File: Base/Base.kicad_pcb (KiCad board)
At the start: 2 copper layers, 72.4 x 72.4 mm, 20 parts, among them J1 USB_C_Receptacle_USB2.0_16P, J2 JST_battery, J3 JST_header, J4 JST_speaker, J5 JST_debug, J6 JST_debug, SW1 SW_power, U1 MCP73831-2-OT, U2 MAX98357A

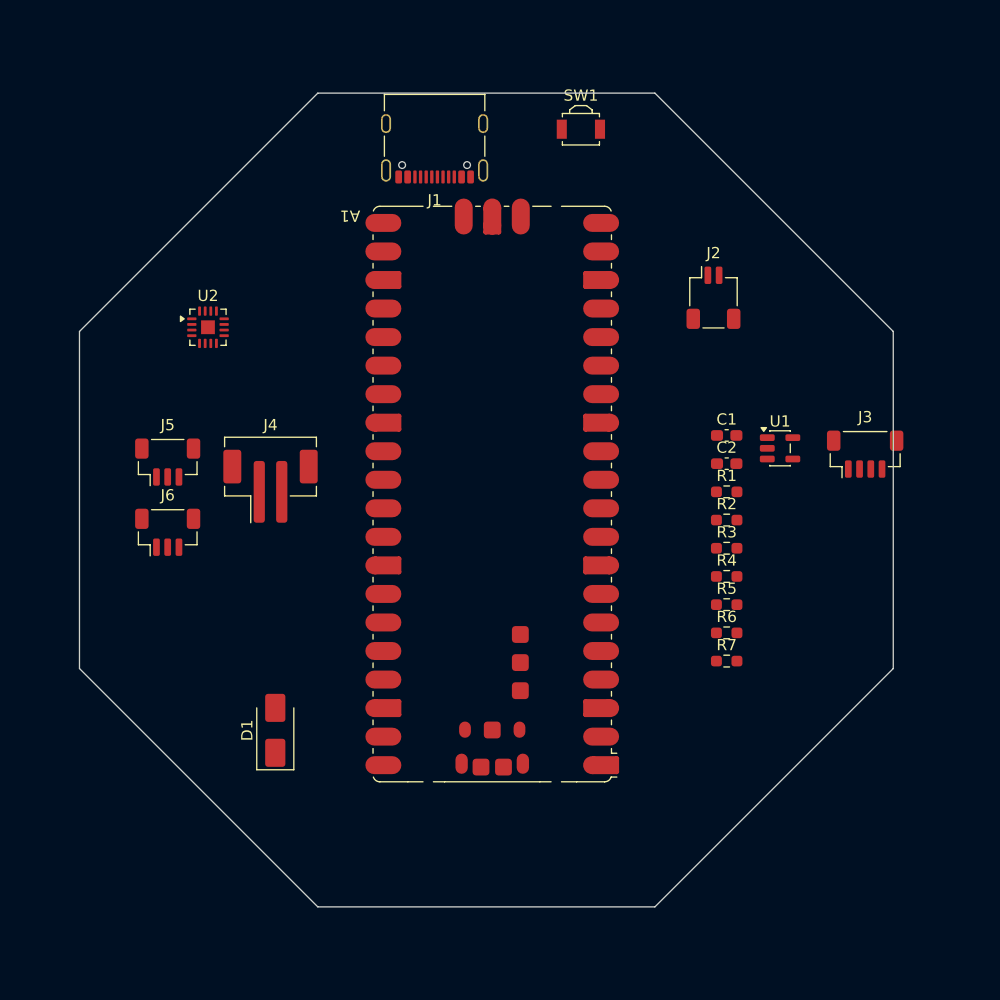
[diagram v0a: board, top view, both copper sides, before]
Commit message: Add LED files, finish base and LED schematics
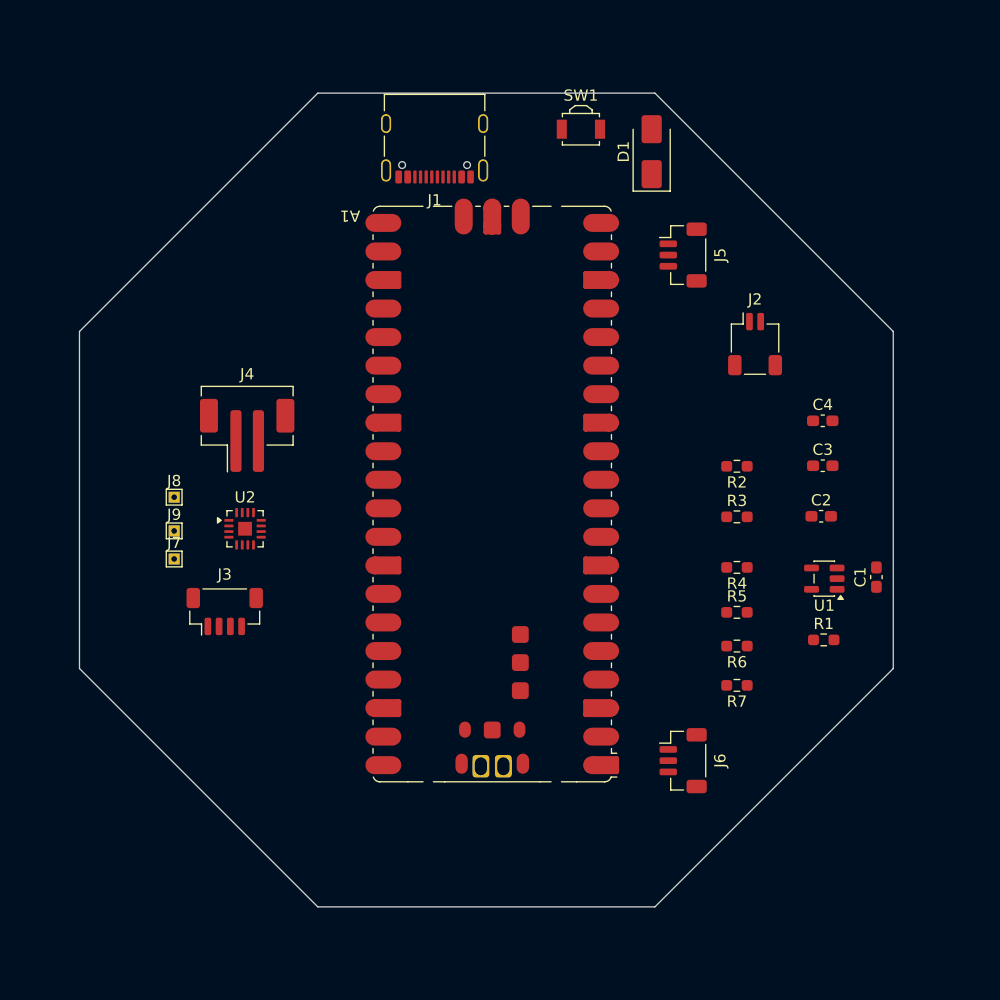
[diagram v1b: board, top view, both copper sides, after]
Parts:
- added C3: 4.7uF, Capacitor_SMD:C_0603_1608Metric_Pad1.08x0.95mm_HandSolder, F.Cu at (186.2, 99.5)
- added C4: 4.7uF, Capacitor_SMD:C_0603_1608Metric_Pad1.08x0.95mm_HandSolder, F.Cu at (186.2, 95.5)
- added J7: Conn_speaker_sd, TestPoint:TestPoint_THTPad_1.0x1.0mm_Drill0.5mm, F.Cu at (128.5, 107.8)
- added J8: Conn_speaker_gain, TestPoint:TestPoint_THTPad_1.0x1.0mm_Drill0.5mm, F.Cu at (128.5, 102.2)
- added J9: Conn_speaker_gnd, TestPoint:TestPoint_THTPad_1.0x1.0mm_Drill0.5mm, F.Cu at (128.5, 105.2)
- added REF**: PicoTestPadHole, Library:PicoTestPadHole, F.Cu at (155.8, 126.2)
- added REF**: PicoTestPadHole, Library:PicoTestPadHole, F.Cu at (157.8, 126.2)
- J5: value JST_debug -> JST_debug_swd
- J6: value JST_debug -> JST_debug_serial
- moved D1 61.4 mm to (171.0, 71.5)
- moved J3 58.7 mm to (133.0, 112.4)
- moved J6 50.2 mm to (173.8, 125.7), turned to -90 degrees
- moved J5 49.4 mm to (173.8, 80.7), turned to -90 degrees
- moved C1 18.3 mm to (191.0, 109.4), turned to 90 degrees
- moved U2 18.2 mm to (134.8, 105.1)
- moved R1 15.8 mm to (186.3, 115.0)
- moved U1 12.3 mm to (186.4, 109.5), turned to 180 degrees
- moved C2 9.63 mm to (186.1, 104.0)
- moved J2 5.54 mm to (180.2, 88.6)
- moved J4 4.98 mm to (135.0, 96.8)
- moved R2 4.87 mm to (178.6, 99.5), turned to 180 degrees
- moved R3 2.94 mm to (178.6, 104.0)
- moved R7 2.35 mm to (178.6, 119.0), turned to 180 degrees
- moved R6 1.49 mm to (178.6, 115.5), turned to 180 degrees
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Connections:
- A1 pad 11: unconnected-(A1-GPIO8-Pad11) -> /WS2812B_DIN
- A1 pad 39: Net-(A1-VSYS) -> /SW_+
- A1 pad 4: unconnected-(A1-GPIO2-Pad4) -> /SPEAKER_SDA
- A1 pad 5: unconnected-(A1-GPIO3-Pad5) -> /SPEAKER_SCL
- A1 pad 6: /WS2812B_DIN -> /SPEAKER_LRC
- D1 pad 1: Net-(A1-VSYS) -> /SW_+
- D1 pad 2: /SW_+ -> Net-(D1-A)
- SW1 pad 2: /SW_+ -> Net-(D1-A)
- U1 pad 1: /STAT_SENSE -> /BAT_STAT
- U2 pad 1: unconnected-(U2-DIN-Pad1) -> /SPEAKER_SDA
- U2 pad 10: unconnected-(U2-OUTN-Pad10) -> /SPEAKER_-
- U2 pad 11: Net-(U2-GND-Pad11) -> /BAT_-
- U2 pad 14: unconnected-(U2-LRCLK-Pad14) -> /SPEAKER_LRC
- U2 pad 15: Net-(U2-GND-Pad11) -> /BAT_-
- U2 pad 16: unconnected-(U2-BCLK-Pad16) -> /SPEAKER_SCL
- U2 pad 2: unconnected-(U2-GAIN_SLOT-Pad2) -> Net-(J8-Pin_1)
- U2 pad 3: Net-(U2-GND-Pad11) -> /BAT_-
- U2 pad 4: unconnected-(U2-~{SD_MODE}-Pad4) -> Net-(J7-Pin_1)
- U2 pad 7: Net-(U2-VDD-Pad7) -> /SW_+
- U2 pad 8: Net-(U2-VDD-Pad7) -> /SW_+
- U2 pad 9: unconnected-(U2-OUTP-Pad9) -> /SPEAKER_+

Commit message: Start work on PCBs, add CC resistors for USB charging
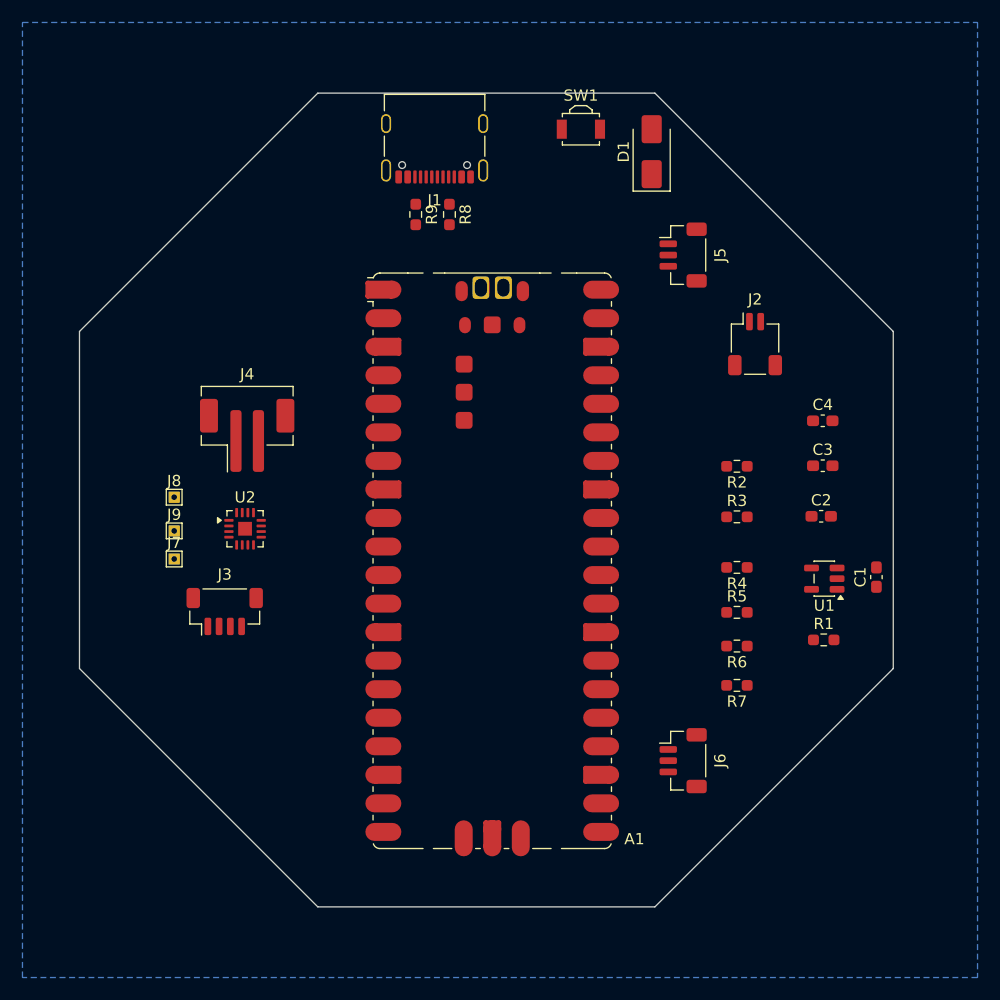
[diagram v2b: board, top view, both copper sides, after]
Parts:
- added R8: 5.1k, Resistor_SMD:R_0603_1608Metric_Pad0.98x0.95mm_HandSolder, F.Cu at (153.0, 77.1)
- added R9: 5.1k, Resistor_SMD:R_0603_1608Metric_Pad0.98x0.95mm_HandSolder, F.Cu at (150.0, 77.1)
- moved REF** 42.6 mm to (155.8, 83.6)
- moved REF** 42.6 mm to (157.8, 83.6)
- moved A1 5.94 mm to (156.8, 107.9), turned to 0 degrees
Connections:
- J1 pad A5: unconnected-(J1-CC1-PadA5) -> Net-(J1-CC1)
- J1 pad B5: unconnected-(J1-CC2-PadB5) -> Net-(J1-CC2)
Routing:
- added copper zone on B.Cu, net /BAT_-

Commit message: Almost finished routing the base PCB except USB
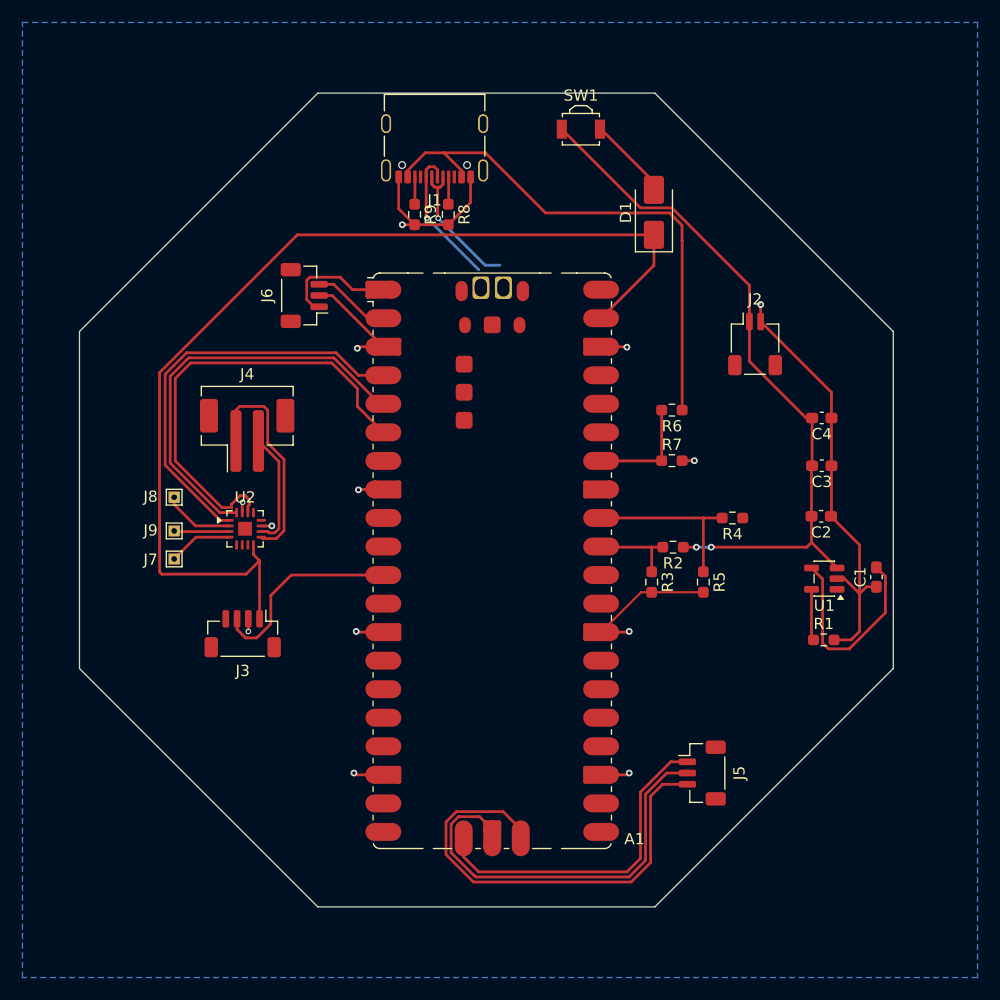
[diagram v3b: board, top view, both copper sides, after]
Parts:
- moved J6 53.4 mm to (140.1, 84.3), turned to 90 degrees
- moved J5 46.1 mm to (175.5, 126.8)
- moved R6 21.8 mm to (172.8, 94.5)
- moved R7 20.8 mm to (172.8, 99.0), turned to 0 degrees
- moved R3 9.55 mm to (171.0, 109.8), turned to -90 degrees
- moved R2 9.18 mm to (172.9, 106.7)
- moved D1 5.40 mm to (171.2, 76.9)
- moved R4 4.42 mm to (178.2, 104.1)
- moved R5 4.03 mm to (175.6, 109.8), turned to -90 degrees
- moved J3 2.54 mm to (134.6, 114.4), turned to 180 degrees
- moved C4 0.26 mm to (186.1, 95.2), turned to 180 degrees
- moved R8 0.10 mm to (152.9, 77.1)
- moved R9 0.10 mm to (149.9, 77.1)
- moved C3 0.09 mm to (186.1, 99.5), turned to 180 degrees
- turned C2 to 180 degrees
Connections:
- A1 pad 32: /USB_SENSE -> /STAT_SENSE
- A1 pad 34: /STAT_SENSE -> /USB_SENSE
- A1 pad TP1: /USB_GND -> /BAT_-
- J1 pad A1: /USB_GND -> /BAT_-
- J1 pad A12: /USB_GND -> /BAT_-
- J1 pad B1: /USB_GND -> /BAT_-
- J1 pad B12: /USB_GND -> /BAT_-
- R7 pad 2: /USB_GND -> /BAT_-
- R8 pad 2: /USB_GND -> /BAT_-
- R9 pad 2: /USB_GND -> /BAT_-
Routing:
- net /BAT_-: track 0.00 -> 134.2 mm, vias 0 -> 13
- net /SW_+: track 0.00 -> 92.5 mm
- net /USB_VBUS: track 0.00 -> 66.2 mm
- net /BAT_+: track 0.00 -> 62.9 mm, vias 0 -> 2
- net /SPEAKER_LRC: track 0.00 -> 40.2 mm
- net /DEBUG_SWDIO: track 0.00 -> 40.1 mm
- net /SPEAKER_SDA: track 0.00 -> 36.8 mm
- net /SPEAKER_SCL: track 0.00 -> 36.8 mm
- net /DEBUG_SWCLK: track 0.00 -> 30.4 mm
- net /SPEAKER_+: track 0.00 -> 19.6 mm
- net /WS2812B_DIN: track 0.00 -> 18.1 mm
- net /STAT_SENSE: track 0.00 -> 15.6 mm
- net /USB_D+: track 0.00 -> 12.7 mm, vias 0 -> 1
- net /USB_D-: track 0.00 -> 12.5 mm, vias 0 -> 1
- net /DEBUG_TX: track 0.00 -> 10.5 mm
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
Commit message: Finish PCB routing
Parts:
- removed REF** (x2): PicoTestPadHole, Library:PicoTestPadHole
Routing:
- net /USB_VBUS: track 66.2 -> 85.0 mm, vias 0 -> 2
- net /BAT_STAT: track 0.00 -> 13.8 mm, vias 0 -> 2
- net /USB_D-: track 12.5 -> 14.5 mm, vias 1 -> 2
- net /USB_D+: track 12.7 -> 14.4 mm, vias 1 -> 2

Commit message: Update after DRC checks, add extra switches for mini hakkero
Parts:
- added J10: JST_switch_1, Connector_JST:JST_SH_SM02B-SRSS-TB_1x02-1MP_P1.00mm_Horizontal, F.Cu at (174.8, 120.3)
- added J11: JST_switch_2, Connector_JST:JST_SH_SM02B-SRSS-TB_1x02-1MP_P1.00mm_Horizontal, F.Cu at (174.7, 114.4)
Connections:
- A1 pad 26: unconnected-(A1-GPIO20-Pad26) -> /BUTTON_1
- A1 pad 27: unconnected-(A1-GPIO21-Pad27) -> /BUTTON_2
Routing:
- net /BAT_-: track 134.2 -> 147.9 mm, vias 13 -> 14
- net /BUTTON_2: track 0.00 -> 7.01 mm
- net /BUTTON_1: track 0.00 -> 6.95 mm
- net /SW_+: track 92.5 -> 93.5 mm
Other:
- board text added: "+ / -"
- board text added: "GAIN GND SD"
- board text added: "Idiots forget this (me) ->"
- board text added: "It ain't magic if it ain't flashy. Danmaku's all about firepower."
- board text added: "SWDIO/GND/SWCLK"
- board text added: "TX/-/RX"

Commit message: Add touch pads for GPIO
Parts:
- added J12: Conn_touch_1, Connector_PinHeader_2.54mm:PinHeader_1x01_P2.54mm_Vertical, F.Cu at (136.6, 120.4)
- added J13: Conn_touch_2, Connector_PinHeader_2.54mm:PinHeader_1x01_P2.54mm_Vertical, F.Cu at (136.6, 126.0)
- added R10: 1M, Resistor_SMD:R_0603_1608Metric_Pad0.98x0.95mm_HandSolder, F.Cu at (131.8, 120.2)
- added R11: 1M, Resistor_SMD:R_0603_1608Metric_Pad0.98x0.95mm_HandSolder, F.Cu at (131.9, 125.9)
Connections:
- A1 pad 16: unconnected-(A1-GPIO12-Pad16) -> /BUTTON_3
- A1 pad 17: unconnected-(A1-GPIO13-Pad17) -> /BUTTON_4
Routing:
- net /BUTTON_3: track 0.00 -> 16.2 mm
- net /BUTTON_4: track 0.00 -> 16.2 mm
- net /BAT_-: track 147.9 -> 150.0 mm, vias 14 -> 16
